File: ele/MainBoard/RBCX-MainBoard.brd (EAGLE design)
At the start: 100 x 100 mm, 191 parts, among them IC1 DRV8833PWP, IC10 INA180A4, IC2 INA180A4, IC3 INA180A4, IC4 DRV8833PWP, IC5 INA180A4, IC6 INA180A4, IC7 INA180A4, IC8 INA180A4, IC9 INA180A4, Q1 CHOOSE_ME, Q3 CHOOSE_ME, Q6 CHOOSE_ME, Q8 CHOOSE_ME, Q9 CHOOSE_ME, U1 STM32F103VCT6, X0 POWER_IN, X1 M3B, X2 M4B, X3 M3B, X4 M4B, X5 POWER_OUT, Y1 3215_2P, Y2 5032/2P

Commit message: MainBoardSCH: Add buttons, LEDs, and UTS connectors
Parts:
- removed C13, C14: 18p, rcl:C0402
- removed C22, C24: 6pF, rcl:C0603
- removed JP19: US4, pinhead:1X04
- removed LED0: RED, led:SML0603
- added BTN1, BTN2, BTN3, BTN4: CHOOSE_ME, Switch:TL3342F160QG/TR
- added C46: 2u2, rcl_upravena:C0603
- added JP10: (no value), pinhead:1X01
- added JP23: BUTTONS, pinhead:2X04
- added LED5: blue, led:CHIP-LED0603
- added R26: 10k, rcl_upravena:R0603
- added R27: 5k6, rcl_upravena:R0603
- added R34, R35, R36, R37: 180R, rcl_upravena:R0603
- added R61, R62, R63, R64, R65, R66, R67, R68: 330R, rcl_upravena:R0603
- C3, C4: value 100n -> 18p; device rcl_upravena:C0402 -> rcl_upravena:C0603
- C5, C8: value 100n -> 6p; device rcl_upravena:C0402 -> rcl_upravena:C0603
- JP13: value US1 -> UTS3
- JP14: value US2 -> UTS4
- JP18: value US3 -> LEDS; device pinhead:1X04 -> pinhead:2X04
- JP4: value (none) -> UTS1; device pinhead:2X04 -> pinhead:1X04
- JP9: value (none) -> UTS2; device pinhead:2X04 -> pinhead:1X04
- LED1: value GREEN -> green; device led:SML0603 -> led:CHIP-LED0603
- LED2: value BLUE -> yellow; device led:SML0603 -> led:CHIP-LED0603
- LED3: value YELLOW -> red; device led:SML0603 -> led:CHIP-LED0603
- R13, R14, R15, R16, R17, R18, R19: value 220 -> 180R; device rcl:R0402 -> rcl_upravena:R0603
- R20: value 1k -> 180R; device rcl:R0402 -> rcl_upravena:R0603
- moved LED1 1114.5 mm to (-137.2, -1079.5)
- moved R14 1076.4 mm to (-97.8, -1059.2)
- moved C8 1073.4 mm to (-97.8, -1054.1), turned to 0 degrees
- moved JP4 1070.1 mm to (-94.0, -1035.0), turned to 0 degrees
- moved C5 1065.0 mm to (-97.8, -1049.0), turned to 0 degrees
- moved C4 1062.4 mm to (-97.8, -1043.9), turned to 0 degrees
- moved C3 1056.1 mm to (-97.8, -1038.9), turned to 0 degrees
- moved JP18 752.8 mm to (-133.3, -1092.2)
- moved JP14 493.4 mm to (-94.0, 152.4)
- moved JP13 473.2 mm to (-94.0, 137.2)
- moved LED2 271.8 mm to (-137.2, 181.6)
- moved LED3 264.1 mm to (-137.2, 193.0), turned to 0 degrees
- moved R20 216.1 mm to (-97.8, 163.8), turned to 0 degrees
- moved R19 215.0 mm to (-97.8, 158.8)
- moved JP9 213.0 mm to (-94.0, 121.9)
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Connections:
- removed net LED0: JP9.1, LED0.A, R17.2
- removed net N$73: JP4.1, JP4.3, JP4.5, JP4.7
- removed net N$75: C8.1
- removed net N$76: C4.1
- removed net N$77: C3.1
- removed net N$78: C5.1
- removed net N$79: LED0.C
- removed net N$80: LED1.C
- removed net N$81: LED2.C
- removed net N$82: LED3.C
- removed net N$83: JP9.7
- removed net N$84: JP9.2, JP9.4, JP9.6, JP9.8
- removed net N$85: JP13.4, JP14.4, JP18.4, JP19.4
- removed net N$9: JP13.1, JP14.1, JP18.1, JP19.1
- removed net SW0: C5.2, JP4.8, R13.2
- removed net SW1: C3.2, JP4.6, R14.2
- removed net SW2: C4.2, JP4.4, R15.2
- removed net SW3: C8.2, JP4.2, R16.2
- removed net US1_ECHO: JP13.3
- removed net US1_TRIG: JP13.2
- removed net US2_ECHO: JP14.3
- removed net US2_TRIG: JP14.2
- removed net US3_ECHO: JP18.3
- removed net US3_TRIG: JP18.2
- removed net US4_ECHO: JP19.3
- removed net US4_TRIG: JP19.2
- removed net VBAT/2: U1.32
- removed net _LED0: R17.1
- removed net _LED1: R18.1
- removed net _LED2: R19.1
- removed net _LED3: R20.1
- removed net _SW0: R13.1
- removed net _SW1: R14.1
- removed net _SW2: R15.1
- removed net _SW3: R16.1
- new net BUTTON-1: BTN1.3, BTN1.4, JP23.1, R34.2
- new net BUTTON-2: BTN2.3, BTN2.4, JP23.3, R35.2
- new net BUTTON-3: BTN3.3, BTN3.4, JP23.5, R36.2
- new net BUTTON-4: BTN4.3, BTN4.4, JP23.7, R37.2
- new net BUTTON1: R34.1
- new net LED-1: JP18.1, R65.2
- new net LED-2: JP18.3, R66.2
- new net LED-3: JP18.5, R67.2
- new net LED-4: JP18.7, R68.2
- new net LED_1: LED1.A, R61.2
- new net LED_2: LED2.A, R62.2
- new net LED_3: LED3.A, R63.2
- new net LED_4: LED5.A, R64.2
- new net N$1: JP10.1, R27.2
- new net UTS1-ECHO: JP4.3, R14.2
- new net UTS1-TRIG: JP4.2, R13.2
- new net UTS2-ECHO: JP9.3, R16.2
- new net UTS2-TRIG: JP9.2, R15.2
- new net UTS3-ECHO: JP13.3, R18.2
- new net UTS3-TRIG: JP13.2, R17.2
- new net UTS4-ECHO: JP14.3, R20.2
- new net UTS4-TRIG: JP14.2, R19.2
- new net V_BAT/2: C46.1, R26.2, R27.1, U1.32
- net +5V0S: now also JP13.1, JP14.1, JP4.1, JP9.1
- net BUTTON2: now also R35.1
- net BUTTON3: now also R36.1
- net BUTTON4: now also R37.1
- net GND: now also BTN1.1, BTN1.2, BTN2.1, BTN2.2, BTN3.1, BTN3.2, BTN4.1, BTN4.2, C3.1, C4.1, C46.2, C5.1, C8.1, JP13.4, JP14.4, JP18.2, JP18.4, JP18.6, JP18.8, JP23.2, JP23.4, JP23.6, JP23.8, JP4.4, JP9.4, LED1.C, LED2.C, LED3.C, LED5.C, R26.1; no longer C13.2, C14.2, C22.2, C24.2
- net LED1: now also R61.1, R65.1; no longer JP9.3, LED1.A, R18.2
- net LED2: now also R62.1, R66.1; no longer JP9.5, LED2.A, R19.2
- net LED3: now also R63.1, R67.1; no longer LED3.A, R20.2
- net LED4: now also R64.1, R68.1
- net OSC32_IN: now also C5.2; no longer C22.1
- net OSC32_OUT: now also C8.2; no longer C24.1
- net OSC_IN: now also C3.2; no longer C13.1
- net OSC_OUT: now also C4.2; no longer C14.1
- net UTS1_ECHO: now also R14.1
- net UTS1_TRIG: now also R13.1
- net UTS2_ECHO: now also R16.1
- net UTS2_TRIG: now also R15.1
- net UTS3_ECHO: now also R18.1
- net UTS3_TRIG: now also R17.1
- net UTS4_ECHO: now also R20.1
- net UTS4_TRIG: now also R19.1
- net VBAT: no longer U1.31
- net V_BAT: now also U1.31
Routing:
- net LED2: track 45.9 -> 0.00 mm
- net SW3: track 44.4 -> 0.00 mm, vias 3 -> 0
- net LED1: track 42.3 -> 0.00 mm
- net LED0: track 38.9 -> 0.00 mm
- net SW1: track 37.4 -> 0.00 mm, vias 3 -> 0
- net SW2: track 36.6 -> 0.00 mm, vias 1 -> 0
- net SW0: track 32.8 -> 0.00 mm, vias 1 -> 0
- net N$83: track 22.8 -> 0.00 mm, vias 1 -> 0
- net LED3: track 2.77 -> 0.00 mm

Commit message: MainBoardSCH: Add coprocessor connectors
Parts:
- added J1: (no value), Wurth_Connectors_WR-USB:632722110112
- added J2: (no value), Wurth_Connectors_WR-USB:614105150621
- added JP19: SWD, pinhead:1X06
- added JP24: STM_CAN, pinhead:1X04
- added JP25: STM_I2C, pinhead:1X04
- added JP32: DEBUG, pinhead:1X04
- added JP33: STM_USART, pinhead:1X07
- added JP34: STM_SPI, pinhead:1X06
- added JP35: STM_ANALOG, pinhead:1X04
- added JP36: USB, pinhead:1X04
- added JP37: usb_id, pinhead:1X01
- added JP38: usb_cc1, pinhead:1X01
- added JP39: usb_sbu1, pinhead:1X01
- added JP40: sbu2, pinhead:1X01
- added JP41: usb_cc2, pinhead:1X01
- added R69, R70, R71, R72, R73, R74, R75, R76, R79, R80, R81, R82, R83, R84, R85, R86, R87, R88, R89, R90, R91: 180R, rcl_upravena:R0603
- added R77, R78: 4k7, rcl_upravena:R0603
- added R92, R93: 1k, rcl_upravena:R0603
- added SJ3, SJ4, SJ5, SJ6: (no value), jumper:SJ_2
- JP10: value (none) -> VBAT/2
- JP15: value (none) -> M12FAULT
- JP31: value (none) -> M34FAULT
- moved JP15 843.7 mm to (-137.2, 254.0)
- moved JP31 525.1 mm to (-137.2, -1287.8)
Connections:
- removed net DAC1: U1.29
- removed net DAC2: U1.30
- removed net ENC3B: D8.3, R31.1, U1.89
- removed net STM_!CS: U1.51
- removed net STM_CK: U1.88
- removed net STM_CTS: U1.84
- removed net STM_MISO: U1.53
- removed net STM_MOSI: U1.54
- removed net STM_RTS: U1.85
- removed net STM_RX: U1.87
- removed net STM_SCK: U1.52
- removed net STM_SCL: U1.92
- removed net STM_SDA: U1.93
- removed net STM_TX: U1.86
- new net DEBUG-RX: JP32.3, R79.2
- new net DEBUG-TX: JP32.4, R80.2
- new net ENC3B/SWO: D8.3, R31.1, R72.1, U1.89
- new net NRST_: JP19.5, R71.2
- new net SSRXN1: J1.B10
- new net SSRXN2: J1.A10
- new net SSRXP1: J1.B11
- new net SSRXP2: J1.A11
- new net SSTXN1: J1.A3
- new net SSTXN2: J1.B3
- new net SSTXP1: J1.A2
- new net SSTXP2: J1.B2
- new net STM-AIO-POWER: JP35.1, SJ6.2
- new net STM-AIO1: JP35.3, R91.2
- new net STM-AIO2: JP35.4, R90.2
- new net STM-CAN-RX: JP24.3, R74.2
- new net STM-CAN-TX: JP24.2, R73.2
- new net STM-I2C-SCL: JP25.3, R76.2, R77.1
- new net STM-I2C-SDA: JP25.4, R75.2, R78.1
- new net STM-SPI-!CS: JP34.6, R89.2
- new net STM-SPI-MISO: JP34.4, R87.2
- new net STM-SPI-SCK: JP34.5, R88.2
- new net STM-SPI_MOSI: JP34.3, R86.2
- new net STM-USART-CK: JP33.7, R85.2
- new net STM-USART-CTS: JP33.5, R83.2
- new net STM-USART-RTS: JP33.6, R84.2
- new net STM-USART-RX: JP33.3, R81.2
- new net STM-USART-TX: JP33.4, R82.2
- new net STM_AIO1: R91.1, U1.29
- new net STM_AIO2: R90.1, U1.30
- new net STM_I2C_PWR: JP25.2, R77.2, R78.2, SJ3.2
- new net STM_I2C_SCL: R76.1, U1.92
- new net STM_I2C_SDA: R75.1, U1.93
- new net STM_SPI_!CS: R89.1, U1.51
- new net STM_SPI_MISO: R87.1, U1.53
- new net STM_SPI_MOSI: R86.1, U1.54
- new net STM_SPI_SCK: R88.1, U1.52
- new net STM_USART_CK: R85.1, U1.88
- new net STM_USART_CTS: R83.1, U1.84
- new net STM_USART_PWR: JP33.1, SJ4.2
- new net STM_USART_PWR1: JP34.1, SJ5.2
- new net STM_USART_RTS: R84.1, U1.85
- new net STM_USART_RX: R81.1, U1.87
- new net STM_USART_TX: R82.1, U1.86
- new net SWCLK_: JP19.2, R69.2
- new net SWDIO_: JP19.4, R70.2
- new net SWO_: JP19.6, R72.2
- new net USBC_SHIELD: J1.S1, J1.S2, J1.S3, J1.S4
- new net USB_CC1: J1.A5, JP38.1, R93.2
- new net USB_CC2: J1.B5, JP41.1, R92.2
- new net USB_ID: J2.4, JP37.1
- new net USB_SBU1: J1.A8, JP39.1
- new net USB_SBU2: J1.B8, JP40.1
- new net UUSB_SHIELD: J2.S1, J2.S2
- new net VUSB: J1.A4, J1.A9, J1.B4, J1.B9, J2.1, JP36.1
- net !M12_FAULT: now also JP15.1; no longer JP31.1
- net !M34_FAULT: now also JP31.1; no longer JP15.1
- net +3V3S: now also JP19.1, JP32.1, SJ3.1, SJ4.1, SJ5.1, SJ6.1
- net +5V0S: now also JP24.1, SJ3.3, SJ4.3, SJ5.3, SJ6.3
- net DEBUG_RX: now also R79.1
- net DEBUG_TX: now also R80.1
- net GND: now also J1.A1, J1.A12, J1.B1, J1.B12, J2.5, JP19.3, JP24.4, JP25.1, JP32.2, JP33.2, JP34.2, JP35.2, JP36.4, R92.1, R93.1
- net NRST: now also R71.1
- net STM_CAN_RX: now also R74.1
- net STM_CAN_TX: now also R73.1
- net SWCLK: now also R69.1
- net SWDIO: now also R70.1
- net USB_DM: now also J1.A7, J1.B7, J2.3, JP36.2
- net USB_DP: now also J1.A6, J1.B6, J2.2, JP36.3

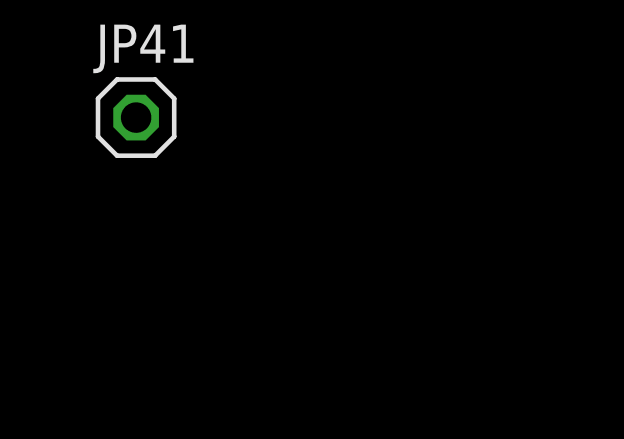
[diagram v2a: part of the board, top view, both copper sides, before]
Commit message: MainBoardSCH: Add ability to redirect DEBUG_TX to SWO signal at SWD connector
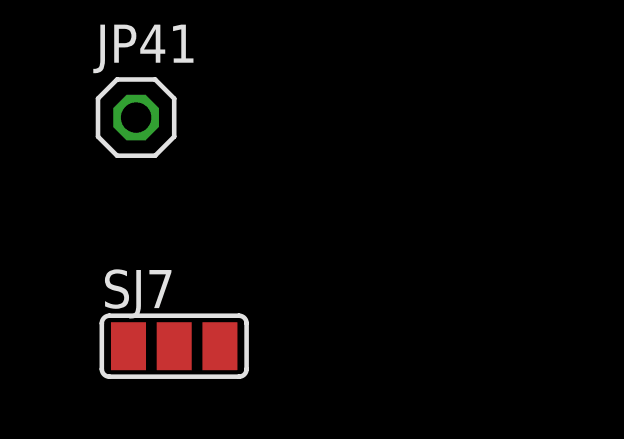
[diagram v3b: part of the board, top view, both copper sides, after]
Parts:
- added SJ7: (no value), jumper:SJ_2
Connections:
- removed net SWO_: JP19.6, R72.2
- new net ENC3-SWO: R72.2, SJ7.3
- new net SWO: JP19.6, SJ7.2
- net DEBUG-TX: now also SJ7.1
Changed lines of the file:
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@@
 <?xml version="1.0" encoding="utf-8"?>
 <!DOCTYPE eagle SYSTEM "eagle.dtd">
-<eagle version="9.5.2">
+<eagle version="9.6.0">
 <drawing>
 <settings>
@@
 <attribute name="VALUE" x="-138.43" y="-1331.595" size="1.27" layer="27"/>
 </element>
+<element name="SJ7" library="jumper" library_urn="urn:adsk.eagle:library:252" package="SJ_2" package3d_urn="urn:adsk.eagle:package:15474/1" value="" x="-135.89" y="-1336.04" smashed="yes">
+<attribute name="NAME" x="-138.303" y="-1334.77" size="1.27" layer="25" ratio="10"/>
+<attribute name="VALUE" x="-135.9901" y="-1336.04" size="0.02" layer="27"/>
+</element>
 </elements>
 <signals>
@@
 <wire x1="-136.31" y1="-1145.54" x2="-127" y2="-1121.41" width="0" layer="19" extent="1-1"/>
 </signal>
-<signal name="SWO_">
-<contactref element="JP19" pad="6"/>
-<contactref element="R72" pad="2"/>
-<wire x1="-136.31" y1="-1150.62" x2="-124.46" y2="-1121.41" width="0" layer="19" extent="1-1"/>
-</signal>
 <signal name="STM-CAN-TX">
 <contactref element="R73" pad="2"/>
@@
 <contactref element="R80" pad="2"/>
 <contactref element="JP32" pad="4"/>
+<contactref element="SJ7" pad="1"/>
+<wire x1="-136.31" y1="-1206.5" x2="-137.414" y2="-1336.04" width="0" layer="19" extent="1-1"/>
 <wire x1="-129.54" y1="-1195.07" x2="-136.31" y2="-1206.5" width="0" layer="19" extent="1-1"/>
 </signal>
@@
 <wire x1="-135.37" y1="-1269.56" x2="-137.16" y2="-1320.8" width="0" layer="19" extent="1-1"/>
 </signal>
+<signal name="ENC3-SWO">
+<contactref element="R72" pad="2"/>
+<contactref element="SJ7" pad="3"/>
+<wire x1="-136.31" y1="-1150.62" x2="-134.366" y2="-1336.04" width="0" layer="19" extent="1-1"/>
+</signal>
+<signal name="SWO">
+<contactref element="SJ7" pad="2"/>
+<contactref element="JP19" pad="6"/>
+<wire x1="-135.89" y1="-1336.04" x2="-124.46" y2="-1121.41" width="0" layer="19" extent="1-1"/>
+</signal>
 </signals>

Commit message: MainBoardSCH: Add draft of ESP pinout
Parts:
- removed JP8: (no value), pinhead:1X15
- removed Q2, Q4, Q5, Q7: (no value), transistors:SOT23
- added D2: SS34, diode:DO214BA
- added R100, R101, R102, R103, R104, R94, R95, R96, R97, R98, R99: 180R, rcl_upravena:R0603
- added SJ10, SJ11, SJ8, SJ9: (no value), jumper:SJ_2
- JP1: value (none) -> STM_CAN; device pinhead:2X04 -> pinhead:1X04
- JP2: value (none) -> STM_I2C; device pinhead:1X15 -> pinhead:1X04
- JP3: value (none) -> STM_USART; device pinhead:1X04 -> pinhead:1X07
- JP5: value (none) -> STM_SPI; device pinhead:2X15 -> pinhead:1X06
- JP7: value (none) -> STM_ANALOG
- R10, R6, R7, R9: value 10k -> 180R; device rcl:R0402 -> rcl_upravena:R0603
- R22, R23: value 10k -> 4k7; device rcl_upravena:R0402 -> rcl_upravena:R0603
- R8: value 10k -> 180R; device rcl_upravena:R0402 -> rcl_upravena:R0603
- moved R23 336.4 mm to (-137.2, 318.8), turned to 0 degrees
- moved JP2 328.0 mm to (-121.9, 297.2), turned to 0 degrees
- moved R22 322.3 mm to (-111.8, 313.7), turned to 0 degrees
- moved JP5 322.2 mm to (-130.8, 289.6)
- moved R8 321.4 mm to (-137.2, 303.5), turned to 0 degrees
- moved R10 292.5 mm to (-124.5, 303.5), turned to 0 degrees
- moved R9 292.4 mm to (-130.8, 303.5), turned to 0 degrees
- moved JP1 282.8 mm to (-133.3, 297.2)
- moved R7 279.9 mm to (-114.3, 295.9), turned to 0 degrees
- moved R6 273.4 mm to (-137.2, 275.6), turned to 0 degrees
- moved JP3 272.1 mm to (-129.5, 281.9)
- moved JP7 264.6 mm to (-116.8, 289.6)
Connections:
- net GPIO34 renamed IN2
- net IO10_NC1 renamed IO7_NC
- net IO11_NC1 renamed IO8_NC
- net IO9_NC1 renamed IO6_NC
- net N$3 renamed EXPANDER_TX
- removed net GPIO12: IM6.13, JP2.6, JP8.6, Q7.2
- removed net GPIO14: IM6.12, JP2.7, JP8.7, Q5.2
- removed net GPIO14_5V: JP1.5, JP3.3, Q5.3, R7.2
- removed net GPIO21: IM6.33, JP2.5, JP8.5
- removed net GPIO25: IM6.9, JP2.10, JP8.10
- removed net GPIO26: IM6.10, JP2.9, JP8.9
- removed net GPIO27: IM6.11, JP2.8, JP8.8
- removed net GPIO32: IM6.7, JP2.12, JP8.12, Q2.2
- removed net GPIO32-5V: JP1.7, JP3.4, Q7.3, R10.2
- removed net GPIO33: IM6.8, JP2.11, JP8.11, Q4.2
- removed net GPIO33-5V: JP1.3, JP3.2, Q4.3, R6.2
- removed net GPIO36: IM6.3, JP2.15, JP8.15
- removed net GPIO39: IM6.4, JP2.14, JP8.14
- removed net IO1: IM6.35, JP2.3, JP8.3
- removed net IO3: IM6.34, JP2.4, JP8.4
- removed net N$60: R8.2
- removed net N$61: R22.2
- removed net N$62: R23.2
- removed net N$63: IM6.19
- removed net N$64: IM6.1
- removed net N$65: R10.1
- removed net N$66: R7.1
- removed net N$67: R6.1
- removed net N$68: R9.1
- removed net N$69: JP1.2, JP1.4, JP1.6, JP1.8
- removed net N$70: JP7.1, JP7.2, JP7.3, JP7.4
- removed net N$71: JP5.10, JP5.12, JP5.14, JP5.16, JP5.18, JP5.2, JP5.20, JP5.22, JP5.24, JP5.26, JP5.28, JP5.30, JP5.4, JP5.6, JP5.8
- removed net N$72: JP5.1, JP5.11, JP5.13, JP5.15, JP5.17, JP5.19, JP5.21, JP5.23, JP5.25, JP5.27, JP5.29, JP5.3, JP5.5, JP5.7, JP5.9
- removed net SCL: IM6.36, JP2.2, JP8.2, R23.1
- removed net SDA: IM6.37, JP2.1, JP8.1, R22.1
- new net DAC1: IM6.9
- new net DAC2: IM6.10
- new net ESP_+5V: D2.C, IM6.19
- new net EXPANDER_RX: IM6.13
- new net GPIO0: IM6.7
- new net GPIO1: IM6.8
- new net I2C_SCL: IM6.36
- new net I2C_SDA: IM6.33
- new net IN1: IM6.6
- new net IN3: IM6.4
- new net IN4: IM6.3
- new net I_LED: IM6.23
- new net N$2: JP3.2
- new net N$3: JP5.2
- new net N$6: JP7.2
- new net SPI_!SS1: IM6.29
- new net SPI_!SS2: IM6.15
- new net SPI_!SS3: IM6.12
- new net SPI_MISO: IM6.31
- new net SPI_MOSI: IM6.37
- new net SPI_SCK: IM6.30
- new net UART2_RX: IM6.27
- new net UART2_TX: IM6.28
- new net UART_AUX: IM6.11
- new net UART_RX: IM6.34
- new net UART_TX: IM6.35
- net +3V3: now also IM6.1; no longer Q2.1, Q4.1, Q5.1, Q7.1
- net +3V3S: now also SJ10.1, SJ11.1, SJ8.1, SJ9.1
- net +5V: now also D2.A
- net +5V0S: now also JP1.1, SJ10.3, SJ11.3, SJ8.3, SJ9.3
- net ESP_BOOT: now also IM6.25
- net ESP_EN: no longer R8.1
- net GND: no longer IM6.6, JP2.13, JP8.13
- net INTELLIGENT_SERVO: now also IM6.26
- net N$4: now also JP2.1; no longer IM6.25
- net N$5: now also JP1.4; no longer JP1.1, JP3.1, Q2.3, R9.2
- net POWER: no longer IM6.15
- net STM-AIO-POWER: now also JP7.1, SJ11.2
- net STM-AIO1: now also JP7.3, R104.2
- net STM-AIO2: now also JP7.4, R103.2
- net STM-CAN-RX: now also JP1.3, R8.2
- net STM-CAN-TX: now also JP1.2, R7.2
- net STM-I2C-SCL: now also JP2.3, R10.2, R22.1
- net STM-I2C-SDA: now also JP2.4, R23.1, R9.2
- net STM-SPI-!CS: now also JP5.6, R102.2
- net STM-SPI-MISO: now also JP5.4, R100.2
- net STM-SPI-SCK: now also JP5.5, R101.2
- net STM-SPI_MOSI: now also JP5.3, R99.2
- net STM-USART-CK: now also JP3.7, R98.2
- net STM-USART-CTS: now also JP3.5, R96.2
- net STM-USART-RTS: now also JP3.6, R97.2
- net STM-USART-RX: now also JP3.3, R94.2
- net STM-USART-TX: now also JP3.4, R95.2
- net STM_I2C_PWR: now also JP2.2, R22.2, R23.2, SJ8.2
- net STM_USART_PWR: now also JP3.1, SJ9.2
- net STM_USART_PWR1: now also JP5.1, SJ10.2
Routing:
- net SDA: track 119.9 -> 0.00 mm, vias 1 -> 0
- net SCL: track 113.6 -> 0.00 mm, vias 1 -> 0
- net GPIO12: track 97.4 -> 0.00 mm, vias 1 -> 0
- net GPIO21: track 87.8 -> 0.00 mm, vias 2 -> 0
- net IO1: track 78.8 -> 0.00 mm, vias 1 -> 0
- net IO3: track 76.5 -> 0.00 mm, vias 1 -> 0
- net GPIO14: track 76.1 -> 0.00 mm
- net GPIO33: track 64.0 -> 0.00 mm
- net GND: track 75.9 -> 14.0 mm
- net GPIO32: track 59.5 -> 0.00 mm
- net GPIO36: track 53.3 -> 0.00 mm
- net GPIO39: track 51.7 -> 0.00 mm
- net N$64: track 51.2 -> 0.00 mm, vias 2 -> 0
- net GPIO25: track 41.5 -> 0.00 mm, vias 1 -> 0
- net GPIO26: track 41.0 -> 0.00 mm, vias 1 -> 0
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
